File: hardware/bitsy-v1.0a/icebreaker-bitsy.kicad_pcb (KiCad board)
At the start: 4 copper layers, 38.1 x 17.8 mm, 101 parts, among them J1 Conn_01x01, J10 Conn_01x01, J11 Conn_01x01, J12 Conn_01x01, J13 Conn_01x01, J14 Conn_01x01, J15 Conn_01x01, J16 Conn_01x01, J17 Conn_01x01, J18 Conn_01x01, J19 Conn_01x01, J2 Conn_01x01, J20 Conn_01x01, J21 Conn_01x01, J22 Conn_01x01, J23 Conn_01x01, J24 Conn_01x01, J25 Conn_01x01, J26 Conn_01x01, J27 Conn_01x01, J28 Conn_01x01, J29 Conn_01x01, J3 Conn_01x01, J30 Conn_01x01, J31 Conn_01x01, J32 Conn_01x01, J33 Conn_01x01, J34 Conn_01x01, J35 Conn_01x01, J36 Conn_01x01, J37 Conn_01x01, J38 Conn_01x01, J39 Conn_01x01, J4 Conn_01x01, J40 Conn_01x01, J5 Conn_01x01, J6 Conn_01x01, J7 Conn_01x01, J8 Conn_01x01, J9 Conn_01x01, P1 USB_C, P2 UP, P3 UP, P4 UP, P5 UP, SW1 TACT, U1 USBLC6-2, U2 TLV75533PDRV, U3 TLV75512PDRV, U4 LY68L6400, U5 W25Q, U6 ICE40UP5K-SG48, X1 DSC6101CI1A-012.0000T

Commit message: WIP placement
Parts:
- removed the C15 at (44.3, 42.3)
- removed C24: 10u, pkl_dipol:C_0603
- removed C27, C30, C31: 100n, pkl_dipol:C_0402
- removed C39: 1u, pkl_dipol:C_0402
- removed D5: RED, pkl_dipol:D_0603
- removed the J24 at (44.0, 39.9)
- removed the J25 at (41.4, 39.9)
- removed J40: Conn_01x01, pkl_pin_headers:Pin_Header_Straight_Round_1x01
- removed the JP2 at (44.9, 52.7)
- removed JP7, JP8, JP9: Jumper, pkl_jumpers:J_NC_0603_30
- removed the R13 at (34.0, 53.3)
- removed R19: 10k, pkl_dipol:R_0402
- removed the R2 at (39.3, 49.0)
- added C1: 4u7, pkl_dipol:C_0603, F.Cu at (22.5, 32.0)
- added C17: 100n, pkl_dipol:C_0402, F.Cu at (46.3, 42.1)
- added C18: 100n, pkl_dipol:C_0402, F.Cu at (53.7, 42.1)
- added C19: 100n, pkl_dipol:C_0402, F.Cu at (47.1, 52.9)
- added C3: 1u, pkl_dipol:C_0402, F.Cu at (39.3, 41.7)
- added C7: 100n, pkl_dipol:C_0402, F.Cu at (44.8, 41.7)
- added D4: FM-B2020RGBA-HG, pkl_led:LED_TRI_2020, F.Cu at (41.6, 45.0)
- added J32: Conn_01x01, pkl_pin_headers:Pin_Header_Straight_Round_1x01, F.Cu at (64.3, 45.0)
- added JP6: Jumper, pkl_jumpers:J_NC_0603_30, B.Cu at (100.9, 46.6)
- added R15: 2k2, pkl_dipol:R_0402, F.Cu at (53.1, 52.9)
- added R5: 22E, pkl_dipol:R_0402, F.Cu at (42.5, 48.0)
- added R9: 10k, pkl_dipol:R_0402, F.Cu at (42.9, 41.7)
- C4: value 100n -> 4u7; footprint pkl_dipol:C_0402 -> pkl_dipol:C_0603
- C8: value 4u7 -> 10u
- D1: value FC-B1010RGBT-HG -> RED; footprint pkl_led:LED_TRI_1010 -> pkl_dipol:D_0603
- JP2: renamed from JP6; moved to B.Cu
- JP3: renamed from JP5; moved to B.Cu
- R11: footprint pkl_dipol:R_Array_Convex_4x0402 -> pkl_dipol:R_0402
- R12: value 2k2 -> 10k
- R3: value 10k -> 5k1
- R6: value 22E -> 1k5
- R8: value 5k1 -> 10k; footprint pkl_dipol:R_0402 -> pkl_dipol:R_Array_Convex_4x0402
- U2: value TLV75533PDRV -> TLV75512PDRV
- U3: value TLV75512PDRV -> TLV75533PDRV
- moved J37 92.7 mm to (154.5, 55.1)
- moved J38 92.7 mm to (151.9, 55.1)
- moved J34 82.7 mm to (146.8, 39.9)
- moved J35 82.6 mm to (146.8, 55.1)
- moved J36 80.0 mm to (144.3, 55.1)
- moved J33 78.5 mm to (141.8, 55.1)
- moved JP4 55.7 mm to (97.4, 39.7)
- moved JP5 55.7 mm to (101.3, 39.7)
- moved R8 51.8 mm to (72.9, 30.1), turned to 270 degrees
- moved JP3 36.5 mm to (90.7, 39.9)
- moved J5 33.9 mm to (64.3, 47.5)
- moved JP2 29.0 mm to (91.2, 44.0), turned to 270 degrees
- moved J26 25.4 mm to (64.3, 39.9)
- moved C6 23.4 mm to (70.9, 30.1)
- moved C4 19.2 mm to (38.9, 45.5), turned to 0 degrees
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- renumbered C35 to C10, C23 to C11, C25 to C12, C28 to C13, C36 to C14, C37 to C15, C38 to C16, C22 to C6, C26 to C9, D4 to D2, J27 to J24, J28 to J25, J29 to J27, J30 to J28, J31 to J29, J32 to J30, J39 to J31, JP3 to JP5, R15 to R13, R5 to R2
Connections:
- net /iUD+ renamed /iD+
- net /iUD- renamed /iD-
- net /xUD+ renamed /xD+
- net /xUD- renamed /xD-
- net /~LEDG renamed /RAM_SS-~LEDG
- net Net-(C35-Pad1) renamed /VPP_2V5
- C2 pad 1: VIN -> +1V2
- C4 pad 1: +3V3 -> VIN
- C8 pad 1: VIN -> /VCCPLL
- C9 pad 1: Net-(C24-Pad1) -> /VCCPLL
- J26 pad 1: /~LED_BLU -> /IOB_20A-~LEDR
- J3 pad 1: +1V2 -> VIN
- J38 pad 1: /FLASH_~HLD~-~RST~-IO3 -> /FLASH_~HLD~-IO3
- J4 pad 1: VIN -> GND
- R10 pad 1: Net-(C24-Pad1) -> /ICEVCC
- R10 pad 2: /ICEVCC -> /VCCPLL
- R11 pad 2: /FLASH_SS -> /iCE_CRESET
- R12 pad 1: +3V3 -> /~UBTN
- R12 pad 2: /iCE_CDONE -> +3V3
- R13 pad 1: Net-(D5-PadA) -> Net-(D1-PadA)
- R3 pad 1: VIN -> GND
- R3 pad 2: Net-(C39-Pad1) -> /CC2
- R6 pad 1: /USB_P -> /USB_DET
- R7 pad 1: +3V3 -> VIN
- R7 pad 2: Net-(R7-Pad2) -> /3V3_EN
- R8 pad 1: GND -> +3V3
- R8 pad 2: /CC2 -> /FLASH_SS
- SW1 pad 1: /~BUTTON -> /~UBTN
- U2 pad 1: +3V3 -> +1V2
- U2 pad 4: Net-(C39-Pad1) -> VIN
- U3 pad 1: +1V2 -> +3V3
- U3 pad 4: VIN -> /3V3_EN
- U4 pad 7: /FLASH_~HLD~-~RST~-IO3 -> /FLASH_~HLD~-IO3
- U5 pad 7: /FLASH_~HLD~-~RST~-IO3 -> /FLASH_~HLD~-IO3
- U6 pad 10: /~BUTTON -> /~UBTN
- U6 pad 11: /~LEDR -> /IOB_20A-~LEDR
- U6 pad 13: /FLASH_~HLD~-~RST~-IO3 -> /FLASH_~HLD~-IO3
- U6 pad 29: Net-(C24-Pad1) -> /VCCPLL
- U6 pad 39: /~LED_RED -> /~RGB0
- U6 pad 40: /~LED_GRN -> /~RGB1
- U6 pad 41: /~LED_BLU -> /~RGB2
- X1 pad 1: Net-(R7-Pad2) -> /CLK_EN
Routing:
- removed copper zone on F.Cu, net +3V3
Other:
- board size 38.1 x 17.8 mm -> 35.6 x 17.8 mm
- board text added: "0"
- board text added: "11"
- board text added: "12"
- board text added: "13"
- board text added: "13 IOB_20A-~LEDR"
- board text added: "14"
- board text added: "14 IOB_23B"
- board text added: "15"
- board text added: "15 IOT_37A"
- board text added: "16"
- board text added: "16 IOT_36B"
- board text added: "17"
- board text added: "17 IOT_39A"
- board text added: "18 IOT_38B"
- board text added: "19 IOT_41A"
- board text added: "20 IOT_42B"
- board text added: "21 IOT_43A"
- board text added: "22 IOT_44B"
- board text added: "23 IOT_48B"
- board text added: "3.3V"
- board text added: "CRESET"
- board text added: "IOB_0A 02"
- board text added: "IOB_13B 08"
- board text added: "IOB_16A 09"
- board text added: "IOB_25B_G3 12"
- board text added: "IOB_29B 11"
- board text added: "IOB_2A 03"
- board text added: "IOB_31B 10"
- board text added: "IOB_3B_G6 00"
- board text added: "IOB_4A 04"
- board text added: "IOB_5B 01"
- board text added: "IOB_6A 05"
- board text added: "IOB_8A 07"
- board text added: "IOB_9B 06"
- board text added: "SS_B/CS xx 39"
- board text added: "V1.0a"
- board text removed: "+3.3V xx 15"
- board text removed: "16 xx GND"
- board text removed: "17 25 IOT_36B"
- board text removed: "18 26 IOT_39A"
- board text removed: "19 27 IOT_38B"
- board text removed: "20 28 IOT_41A"
- board text removed: "21 31 IOT_42B"
- board text removed: "22 32 IOT_43A"
- board text removed: "23 34 IOT_44B"
- board text removed: "24"
- board text removed: "24 36 IOT_48B"
- board text removed: "25"
- board text removed: "27"
- board text removed: "27 41 ~LED_BLU"
- board text removed: "28 xx +3.3V"
- board text removed: "29 xx GND"
- board text removed: "30 xx VIN"
- board text removed: "36 20 IOB_25B_G3"
- board text removed: "38 21 IOB_23B"
- board text removed: "39 xx SS_B/CS"
- board text removed: "40 23 IOT_37A"
- board text removed: "CDONE xx 33"
- board text removed: "CRESET xx 35"
- board text removed: "G"
- board text removed: "GND xx 01"
- board text removed: "IOB_0A 46 04"
- board text removed: "IOB_13B 06 10"
- board text removed: "IOB_16A 09 11"
- board text removed: "IOB_29B 19 34"
- board text removed: "IOB_2A 47 05"
- board text removed: "IOB_31B 18 32"
- board text removed: "IOB_3B_G6 44 02"
- board text removed: "IOB_4A 48 06"
- board text removed: "IOB_5B 45 03"
- board text removed: "IOB_6A 02 07"
- board text removed: "IOB_8A 04 09"
- board text removed: "IOB_9B 03 08"
- board text removed: "LEDB"
- board text removed: "LEDG"
- board text removed: "LEDR"
- board text removed: "N"
- board text removed: "V0.3a"

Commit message: Programming header ideas
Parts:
- removed J33, J35, J36, J37, J38: Conn_01x01, pkl_pin_headers:Pin_Header_Straight_Round_1x01
- removed the J34 at (146.8, 39.9)
- added P10: POGO_PAD_SMD, pkl_pads:POGO_PAD_SMD_R_1x1, B.Cu at (79.5, 50.0)
- added P5: POGO_PAD_SMD, pkl_pads:POGO_PAD_SMD_R_1x1, B.Cu at (79.5, 42.4)
- added P6: POGO_PAD_SMD, pkl_pads:POGO_PAD_SMD_R_1x1, B.Cu at (79.5, 45.0)
- added P7: POGO_PAD_SMD, pkl_pads:POGO_PAD_SMD_R_1x1, B.Cu at (79.5, 47.5)
- added P8: POGO_PAD_SMD, pkl_pads:POGO_PAD_SMD_R_1x1, B.Cu at (82.1, 52.6)
- added P9: POGO_PAD_SMD, pkl_pads:POGO_PAD_SMD_R_1x1, B.Cu at (79.5, 52.6)
- added REF**: PinHeader_2x05_P2.54mm_Vertical_SMD, Connector_PinHeader_2.54mm:PinHeader_2x05_P2.54mm_Vertical_SMD, B.Cu at (61.1, 47.5)
- renumbered P1 to J34, P2 to P1, P3 to P2, P4 to P3, P5 to P4

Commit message: Tentatively finished component placement
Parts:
- removed P10, P5, P6, P7, P8, P9: POGO_PAD_SMD, pkl_pads:POGO_PAD_SMD_R_1x1
- removed the REF** at (61.1, 47.5)
- added J33: Conn_02x05_Odd_Even, Connector_PinHeader_2.54mm:PinHeader_2x05_P2.54mm_Vertical_SMD, B.Cu at (61.1, 47.5)
- U5: footprint pkl_housings_soic:SOIC-8_5.3x5.3mm_Pitch1.27mm -> Package_SO:SOIC-8_5.275x5.275mm_P1.27mm
- X1: value DSC6101CI1A-012.0000T -> 12MHz
- moved JP4 47.8 mm to (143.3, 26.3)
- moved JP6 47.8 mm to (146.8, 33.2)
- moved JP2 47.8 mm to (137.1, 30.6)
- moved JP3 47.8 mm to (136.6, 26.4)
- moved JP5 47.8 mm to (147.2, 26.3)
- moved C2 26.3 mm to (44.5, 51.4), turned to 270 degrees
- moved U2 25.6 mm to (43.8, 48.9)
- moved C1 25.5 mm to (41.3, 49.3), turned to 180 degrees
- moved R8 22.0 mm to (59.2, 47.3), turned to 90 degrees
- moved C6 21.9 mm to (57.3, 47.3), turned to 90 degrees
- moved D3 16.5 mm to (61.8, 47.5), turned to 180 degrees
- moved C10 3.61 mm to (54.9, 42.1), turned to 90 degrees
- moved R6 3.54 mm to (42.0, 45.5), turned to 270 degrees
- moved R2 3.52 mm to (41.0, 45.5), turned to 270 degrees
- moved D4 2.34 mm to (43.8, 45.8)
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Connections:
- D4 pad 1: +3V3 -> /~RGB0
- D4 pad 3: /~RGB1 -> +3V3
- D4 pad 4: /~RGB0 -> /~RGB1
- R11 pad 1: +3V3 -> /iCE_CRESET
- R11 pad 2: /iCE_CRESET -> +3V3
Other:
- board text removed: "25 39 ~LED_RED"
- board text removed: "26 40 ~LED_GRN"

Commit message: Begin routing
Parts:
- moved JP5 102.4 mm to (46.8, 46.3), turned to 180 degrees
- moved JP6 101.2 mm to (46.8, 48.7)
- moved JP4 98.8 mm to (46.8, 47.5), turned to 180 degrees
- moved JP2 83.8 mm to (55.0, 47.5), turned to 180 degrees
- moved JP3 83.7 mm to (55.0, 45.0)
- moved REF** 30.3 mm to (73.3, 65.4)
- moved R11 19.0 mm to (71.1, 52.5)
- moved R15 15.9 mm to (69.0, 52.7)
- moved R10 3.80 mm to (54.3, 42.1)
- moved C7 3.72 mm to (41.8, 41.7), turned to 180 degrees
- moved C18 3.67 mm to (54.6, 45.7), turned to 0 degrees
- moved C10 2.02 mm to (54.6, 44.1), turned to 0 degrees
- moved R9 1.92 mm to (42.3, 43.2), turned to 270 degrees
- moved C14 1.00 mm to (50.1, 52.9)
- moved C15 1.00 mm to (49.1, 52.9)
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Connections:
- D4 pad 1: /~RGB0 -> /~RGB2
- D4 pad 2: /~RGB2 -> /~RGB0
- R10 pad 1: /ICEVCC -> /VCCPLL
- R10 pad 2: /VCCPLL -> /ICEVCC
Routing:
- net GND: track 0.00 -> 24.4 mm, vias 0 -> 5
- net /SHIELD: track 0.00 -> 18.7 mm
- net /IOB_3B_G6: track 0.00 -> 15.1 mm, vias 0 -> 1
- net /IOB_5B: track 0.00 -> 12.4 mm, vias 0 -> 1
- net +3V3: track 0.00 -> 10.5 mm
- net /IOB_0A: track 0.00 -> 9.64 mm, vias 0 -> 1
- net /ICEVCC: track 0.00 -> 9.64 mm, vias 0 -> 3
- net /IOT_48B: track 0.00 -> 9.61 mm, vias 0 -> 1
- net /IOT_44B: track 0.00 -> 8.24 mm, vias 0 -> 1
- net /IOB_16A: track 0.00 -> 7.99 mm, vias 0 -> 1
- net /IOB_8A: track 0.00 -> 7.79 mm
- net /~UBTN: track 0.00 -> 7.79 mm, vias 0 -> 1
- net /IOB_13B: track 0.00 -> 7.60 mm, vias 0 -> 1
- net VIN: track 0.00 -> 7.55 mm, vias 0 -> 1
- net /IOB_2A: track 0.00 -> 7.48 mm, vias 0 -> 1
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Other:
- net class Default: via_drill 0.3 -> 0.25
- net class S50 added: clearance 0.15, trace_width 0.3, via_dia 0.5, via_drill 0.25
- net class USB-D90 added: clearance 0.15, trace_width 0.275, via_dia 0.5, via_drill 0.25
- rule via_min_drill: 0.3 -> 0.25

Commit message: Routing WIP
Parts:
- removed the C10 at (54.6, 44.1)
- removed the C18 at (54.6, 45.7)
- removed the C19 at (46.3, 52.9)
- added C11: 100n, pkl_dipol:C_0402, F.Cu at (54.6, 45.7)
- added C12: 100n, pkl_dipol:C_0402, F.Cu at (46.9, 52.9)
- added C7: 100n, pkl_dipol:C_0402, F.Cu at (53.2, 52.9)
- added C9: DNP, pkl_dipol:C_0402, F.Cu at (54.0, 43.6)
- moved JP3 23.4 mm to (78.0, 49.5)
- moved JP2 18.9 mm to (72.4, 54.9)
- moved R11 18.3 mm to (55.1, 43.6), turned to 90 degrees
- moved R15 17.3 mm to (55.7, 41.7), turned to 180 degrees
- moved JP4 11.2 mm to (47.7, 58.7)
- moved JP6 10.6 mm to (50.3, 58.7)
- moved R8 7.14 mm to (64.1, 52.5), turned to 180 degrees
- moved D3 5.60 mm to (61.9, 41.9), turned to 0 degrees
- moved R10 3.40 mm to (50.9, 42.1)
- moved C6 2.21 mm to (55.1, 47.1)
- moved U4 1.60 mm to (59.3, 45.4), turned to 180 degrees
- moved C19 1.00 mm to (51.9, 42.1)
- moved C20 1.00 mm to (53.6, 41.9)
- moved C13 0.50 mm to (48.6, 52.9)
- moved C14 0.50 mm to (49.6, 52.9)
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- renumbered C17 to C10, C16 to C13, C15 to C14, C14 to C15, C13 to C16, C12 to C17, C11 to C18, C9 to C19, C8 to C20, C7 to C8
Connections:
- R8 pad 2: /FLASH_SS -> /FLASH_~HLD~-IO3
- R8 pad 4: /FLASH_~HLD~-IO3 -> /FLASH_SS
- R8 pad 6: /FLASH_~WP~-IO2 -> /iCE_SCK
- R8 pad 8: /iCE_SCK -> /FLASH_~WP~-IO2
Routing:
- net /IOB_25B_G3: track 0.00 -> 18.1 mm, vias 0 -> 1
- net /IOB_29B: track 0.00 -> 14.2 mm, vias 0 -> 1
- net /FLASH_~HLD~-IO3: track 0.00 -> 12.1 mm
- net /iCE_SCK: track 0.00 -> 11.9 mm
- net /IOB_31B: track 0.00 -> 11.4 mm, vias 0 -> 1
- net /FLASH_MISO-IO1: track 0.00 -> 10.5 mm
- net +3V3: track 10.5 -> 19.8 mm, vias 0 -> 2
- net /iCE_CDONE: track 0.90 -> 9.77 mm
- net GND: track 24.4 -> 33.2 mm, vias 5 -> 10
- net /iCE_CRESET: track 2.80 -> 10.5 mm
- net /FLASH_~WP~-IO2: track 0.00 -> 3.12 mm, vias 0 -> 1
- net /VCCIO_01: track 3.31 -> 5.34 mm, vias 1 -> 2
- net /VCCPLL: track 5.83 -> 4.01 mm
- net /FLASH_SS: track 0.00 -> 1.66 mm
- net /VPP_2V5: track 0.00 -> 1.46 mm, vias 0 -> 1
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- removed copper zone on F.Cu, net GND

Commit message: More routing WIP
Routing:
- net VBUS: track 1.09 -> 3.49 mm, vias 1 -> 3
- net GND: track 33.2 -> 34.4 mm, vias 10 -> 11
- removed copper zone on In1.Cu, net /SHIELD

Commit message: Almost done routing!
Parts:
- removed REF**: null_Logo_SilkS_6.5mm, pkl_logos:null_Logo_SilkS_6.5mm
- added JP6: Jumper, pkl_jumpers:J_NC_0603_30, B.Cu at (56.2, 46.2)
- added LOGO1: 1BitSquared, pkl_logos:null_Logo_SilkS_6.5mm, B.Cu at (49.5, 47.5)
- J1, J2: value Conn_01x01 -> 3V3
- J10: value Conn_01x01 -> 4
- J11: value Conn_01x01 -> 1
- J12: value Conn_01x01 -> 5
- J13: value Conn_01x01 -> 7
- J14: value Conn_01x01 -> 6
- J15: value Conn_01x01 -> 16
- J16: value Conn_01x01 -> 15
- J17: value Conn_01x01 -> 18
- J18: value Conn_01x01 -> 17
- J19: value Conn_01x01 -> 19
- J20: value Conn_01x01 -> 20
- J21: value Conn_01x01 -> 21
- J22: value Conn_01x01 -> 22
- J23: value Conn_01x01 -> 23
- J24: value Conn_01x01 -> 8
- J25: value Conn_01x01 -> 9
- J26: value Conn_01x01 -> 13
- J27: value Conn_01x01 -> 14
- J28: value Conn_01x01 -> 12
- J29: value Conn_01x01 -> 11
- J3: value Conn_01x01 -> VIN
- J30: value Conn_01x01 -> 10
- J31: value Conn_01x01 -> CDONE
- J32: value Conn_01x01 -> CRESET
- J34: renamed from J33; value Conn_02x05_Odd_Even -> PROG; footprint Connector_PinHeader_2.54mm:PinHeader_2x05_P2.54mm_Vertical_SMD -> pkl_pin_headers:PinHeader_2x05_P2.54mm_Vertical_SMD
- J4, J5, J6: value Conn_01x01 -> GND
- J7: value Conn_01x01 -> 2
- J8: value Conn_01x01 -> 3
- J9: value Conn_01x01 -> 0
- P1, P2, P3, P4: footprint pkl_pads:PAD_SMD_1x2.65 -> pkl_pads:PAD_SMD_1x2.65_ROUNDED
- moved JP3 24.3 mm to (54.5, 43.2)
- moved JP2 18.1 mm to (54.5, 52.0)
- moved JP7 9.91 mm to (43.0, 52.0)
- moved JP4 6.70 mm to (47.8, 52.0)
- moved JP1 5.16 mm to (36.9, 44.5), turned to 0 degrees
- moved JP5 4.33 mm to (44.0, 43.0)
- moved J34 0.64 mm to (60.5, 47.5)
- renumbered J34 to J33, JP6 to JP7
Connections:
- net /ICEVCC renamed VCC
- C10 pad 1: /VCCIO_01 -> /VCCIO_0
- C11 pad 1: /VCCIO_01 -> /VCCIO_1
- J34 pad 10: /FLASH_~WP~-IO2 -> /FLASH_~HLD~-IO3
- J34 pad 6: /FLASH_MOSI-IO0 -> /FLASH_MISO-IO1
- J34 pad 8: /FLASH_~HLD~-IO3 -> /FLASH_MOSI-IO0
- J34 pad 9: /FLASH_MISO-IO1 -> /FLASH_~WP~-IO2
- JP5 pad 1: /VCCIO_01 -> /VCCIO_0
- U6 pad 22: /VCCIO_01 -> /VCCIO_1
- U6 pad 33: /VCCIO_01 -> /VCCIO_0
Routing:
- net VIN: track 7.55 -> 23.7 mm, vias 1 -> 2
- net VBUS: track 3.49 -> 16.3 mm
- net /IOT_48B: track 9.61 -> 0.59 mm
- net /IOT_44B: track 8.24 -> 0.00 mm, vias 1 -> 0
- net +3V3: track 19.8 -> 25.2 mm, vias 2 -> 6
- net /VCCIO_01: track 5.34 -> 0.00 mm, vias 2 -> 0
- net /VCCIO_0: track 0.00 -> 4.98 mm, vias 0 -> 1
- net /xD-: track 3.94 -> 8.89 mm, vias 0 -> 1
- net /xD+: track 4.93 -> 9.88 mm, vias 0 -> 1
- net /VCCIO_1: track 0.00 -> 3.59 mm, vias 0 -> 1
- net VCC: track 10.1 -> 13.4 mm
- net +1V2: track 1.92 -> 4.74 mm
- net /VCCIO_2: track 2.26 -> 4.98 mm
- net /IOB_31B: track 11.4 -> 13.6 mm
- net GND: track 34.4 -> 36.0 mm, vias 11 -> 13
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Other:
- board text added: "1v2"
- board text added: "2020"
- board text added: "3v3"
- board text added: "CC BY-SA"
- board text added: "Cdone"
- board text added: "Cres"
- board text added: "D+"
- board text added: "D-"
- board text added: "G"
- board text added: "IO0"
- board text added: "IO1"
- board text added: "IO2"
- board text added: "IO3"
- board text added: "MISO"
- board text added: "MOSI"
- board text added: "SCK"
- board text added: "SPI Flash Prog"
- board text added: "SS"
- board text added: "V"
- board text added: "VBUS"
- board text added: "Vcc"
- board text added: "Vpp 2v5"
- board text removed: "1Bitsquared 2020"
- board text removed: "1V2"
- board text removed: "37 xx SCK"
- board text removed: "3V3"
- board text removed: "C"
- board text removed: "CC-BY-SA"
- board text removed: "D"
- board text removed: "FLASH_MISO/IO1 xx 14"
- board text removed: "FLASH_MOSI/IO0 xx 31"
- board text removed: "I"
- board text removed: "ICESS"
- board text removed: "IOB_22A FLASH_~WP~/IO2 12 13"
- board text removed: "IOB_24A FLASH_~HLD~/~RST~/IO3 13 12"
- board text removed: "K"
- board text removed: "O"
- board text removed: "R"
- board text removed: "S"
- board text removed: "SS_B/CS xx 39"
- board text removed: "VCCIO01"
- board text removed: "VCCIO2"
- board text removed: "vpp2v5"

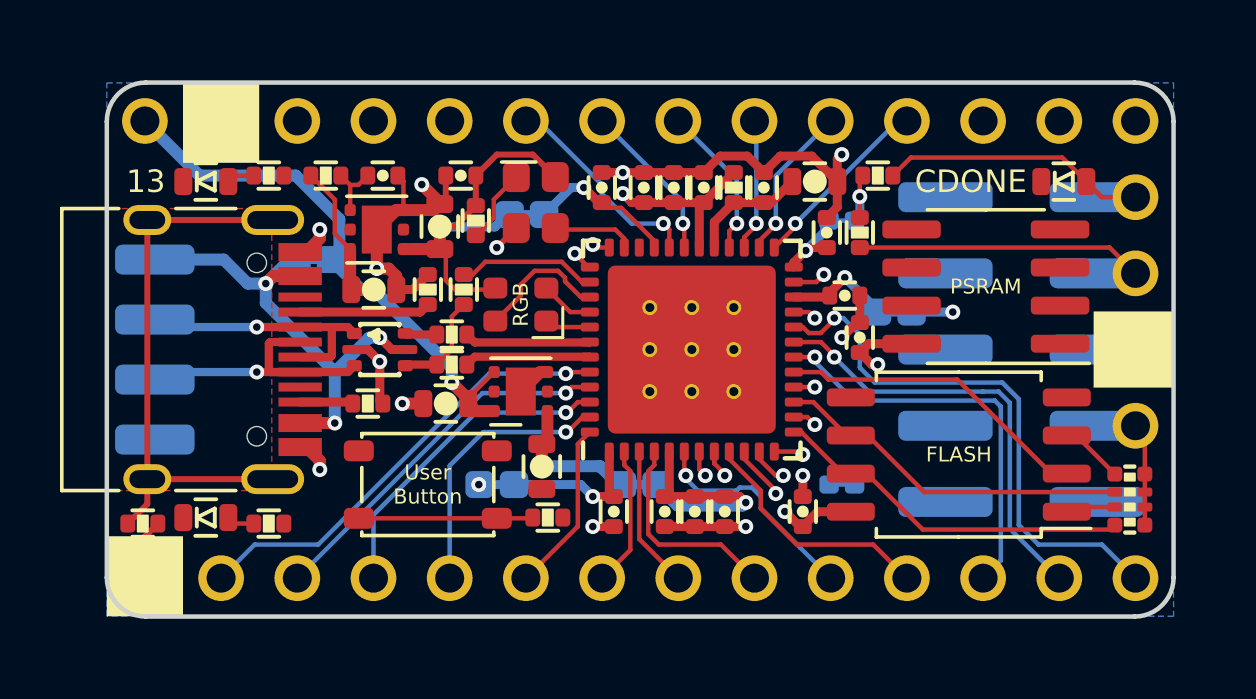
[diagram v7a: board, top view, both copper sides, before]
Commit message: One net left to route
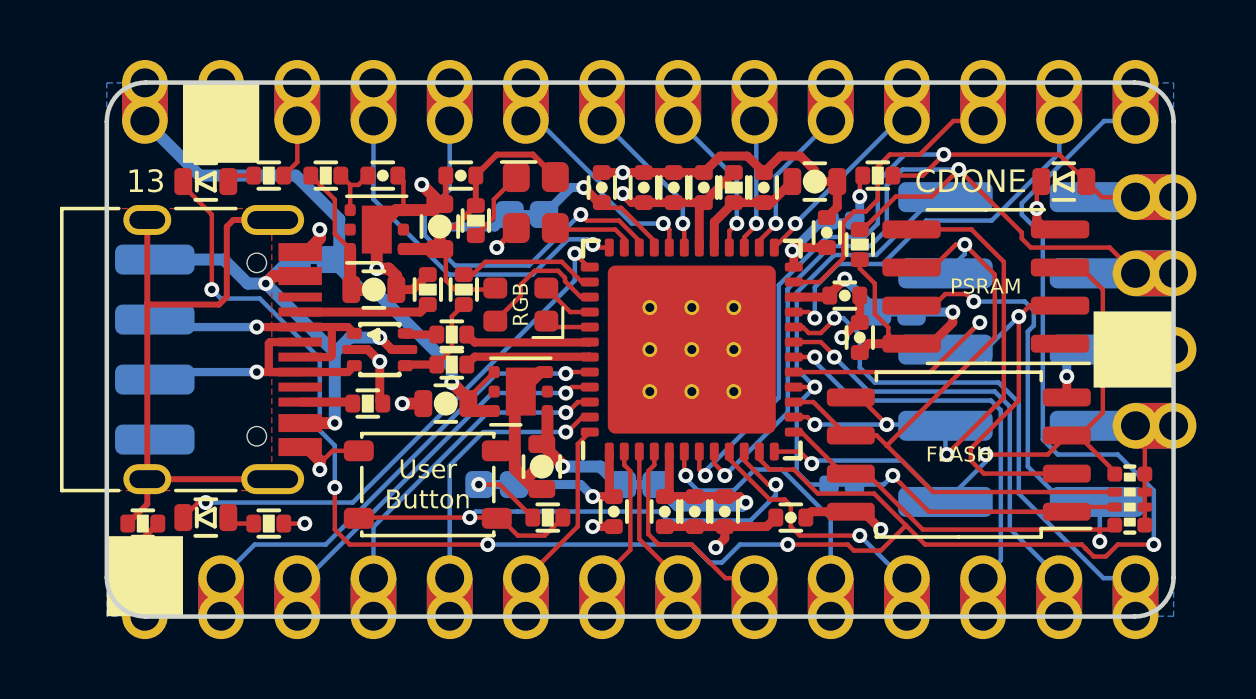
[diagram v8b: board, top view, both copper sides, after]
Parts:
- J1, J10, J11, J12, J13, J14, J15, J16, J17, J18, J19, J2, J20, J21, J22, J23, J24, J25, J26, J27, J28, J29, J3, J30, J31, J32, J4, J5, J6, J7, J8, J9: footprint pkl_pin_headers:Pin_Header_Straight_Round_1x01 -> pkl_pin_headers:Pin_Header_Straight_Round_1x01_Castellated
- moved C7 0.45 mm to (52.8, 53.1), turned to 180 degrees
- moved R11 0.40 mm to (55.1, 44.0), turned to 270 degrees
- turned J1 to 180 degrees
- turned J15 to 180 degrees
- turned J16 to 180 degrees
- turned J17 to 180 degrees
- turned J18 to 180 degrees
- turned J19 to 180 degrees
- turned J2 to 90 degrees
- turned J20 to 180 degrees
- turned J21 to 180 degrees
- turned J22 to 180 degrees
- turned J23 to 180 degrees
- turned J26 to 180 degrees
- turned J27 to 180 degrees
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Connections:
- J34 pad 10: /FLASH_~HLD~-IO3 -> /FLASH_~WP~-IO2
- J34 pad 9: /FLASH_~WP~-IO2 -> /FLASH_~HLD~-IO3
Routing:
- net /IOB_20A-~LEDR: track 1.28 -> 68.8 mm, vias 1 -> 5
- net /FLASH_~WP~-IO2: track 3.12 -> 22.1 mm, vias 1 -> 2
- net /iCE_CRESET: track 10.5 -> 28.2 mm, vias 1 -> 2
- net /FLASH_MOSI-IO0: track 0.80 -> 18.5 mm, vias 1 -> 3
- net /RAM_SS-~LEDG: track 0.69 -> 17.9 mm, vias 1 -> 2
- net /iCE_CDONE: track 9.77 -> 25.3 mm, vias 1 -> 2
- net /FLASH_~HLD~-IO3: track 12.1 -> 26.4 mm, vias 0 -> 2
- net /iCE_SS_B: track 0.70 -> 14.6 mm
- net /IOT_44B: track 0.00 -> 13.0 mm, vias 0 -> 1
- net /~UBTN: track 7.65 -> 20.1 mm, vias 1 -> 2
- net /IOB_23B: track 0.78 -> 12.9 mm
- net /iCE_SCK: track 11.9 -> 23.9 mm, vias 0 -> 1
- net GND: track 36.0 -> 47.8 mm, vias 13 -> 15
- net /IOT_48B: track 0.59 -> 12.1 mm
- net /FLASH_MISO-IO1: track 10.5 -> 21.7 mm, vias 0 -> 2
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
